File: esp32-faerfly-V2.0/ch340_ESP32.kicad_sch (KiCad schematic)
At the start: 9 parts, among them Q1 BC817, Q2 BC817, SW2 BOOT, SW3 EN, U4 CH340C

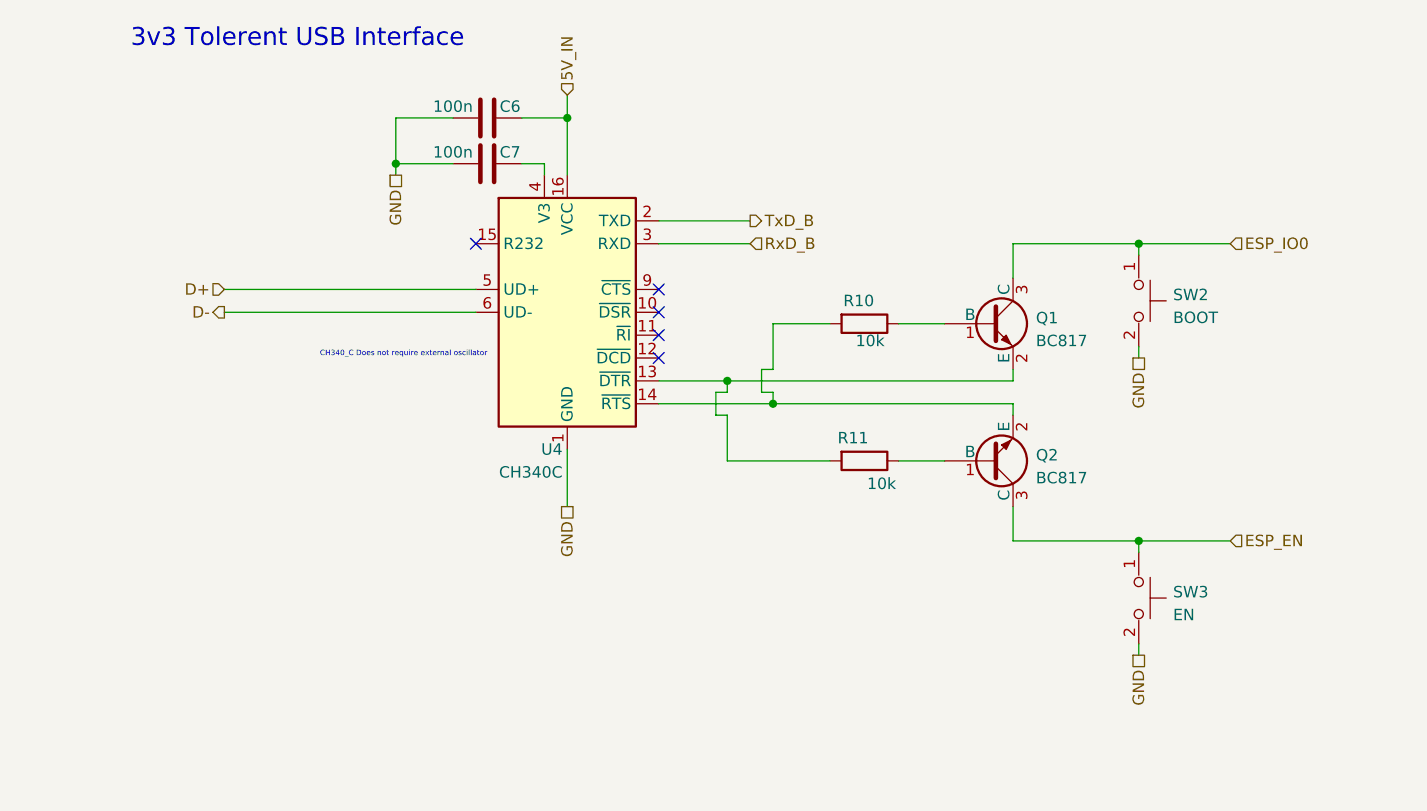
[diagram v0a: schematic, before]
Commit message: started adding modifcations for V2 see changelog
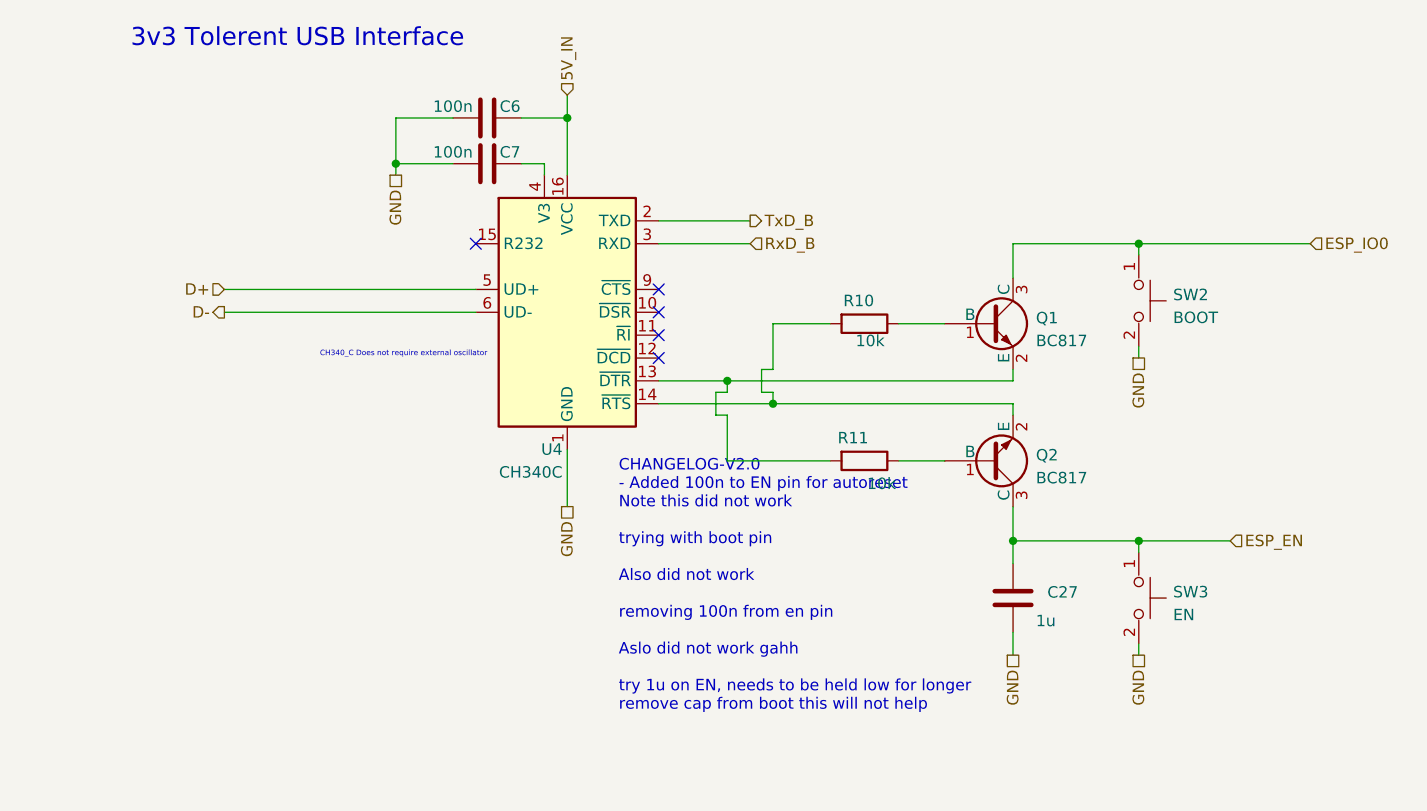
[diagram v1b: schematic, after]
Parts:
- added C27: 1u, Capacitor_SMD:C_0805_2012Metric_Pad1.18x1.45mm_HandSolder, symbol 000_Capacitor_Film_Immo:cap_film_0805
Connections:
- net ESP_EN: now also C27.1
- net GND: now also C27.2
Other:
- note added: "CHANGELOG-V2.0 - Added 100n to EN pin for autoreset Note this did not work trying with boot pin Also did not work removing 100n from en pin Aslo did not work gahh try 1u on EN, needs to be held low for longer remove cap from boot this will not help"
